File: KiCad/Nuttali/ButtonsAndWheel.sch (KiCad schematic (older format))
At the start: 17 parts, among them J3 Conn_01x03_Male, SW8 Rotary_Encoder, U6 Button, U7 Button, U8 Scroll_button, U9 Button

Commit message: Finnished design.
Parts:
- removed D4: LED, Nuttali:LED, symbol Nuttali-rescue:LED-Device
- added J4: Conn_01x02_Male, Connector_PinSocket_2.54mm:PinSocket_1x02_P2.54mm_Vertical, symbol Connector:Conn_01x02_Male
- added TP10, TP11, TP12, TP13, TP14, TP15: TestPoint, TestPoint:TestPoint_Pad_1.0x1.0mm, symbol Nuttali-rescue:TestPoint-Connector
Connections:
- net GND: now also J4.1 (Pin_1)
- net LeftB: now also TP10.1
- net RightB: now also TP11.1
- net Turbo: now also TP15.1
- net Turbo_LED: now also J4.2 (Pin_2)
- net WheelA: now also TP13.1
- net WheelB: now also TP14.1
- net WheelButton: now also TP12.1
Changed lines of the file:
@@
 Wire Wire Line
 	5000 2550 4950 2550
-Wire Wire Line
-	3900 2750 3800 2750
-Text GLabel 3800 2750 0    50   Output ~ 0
+Text GLabel 3650 2750 0    50   Output ~ 0
 WheelButton
 $Comp
@@
 $EndComp
 $Comp
-L Nuttali-rescue:LED-Device D4
-U 1 1 602CBCDE
-P 9600 2650
-F 0 "D4" H 9593 2395 50  0000 C CNN
-F 1 "LED" H 9593 2486 50  0000 C CNN
-F 2 "Nuttali:LED" H 9600 2650 50  0001 C CNN
-F 3 "~" H 9600 2650 50  0001 C CNN
-	1    9600 2650
-	-1   0    0    1
-$EndComp
-$Comp
 L Nuttali-rescue:GND-power #PWR0152
 U 1 1 602CF144
@@
 Text GLabel 9300 2650 0    50   Input ~ 0
 Turbo_LED
-Wire Wire Line
-	9300 2650 9450 2650
-Wire Wire Line
-	9750 2650 10100 2650
 Wire Wire Line
 	10100 2700 10100 2650
@@
 Connection ~ 1150 2950
 Wire Wire Line
-	1150 2950 850  2950
+	1150 2950 900  2950
 $Comp
 L Nuttali-rescue:R-Device R7
@@
 $EndComp
 Wire Wire Line
-	900  1350 1200 1350
+	900  1350 950  1350
 Connection ~ 1200 1350
 Wire Wire Line
@@
 	7000 6500 7000 500
 Wire Wire Line
-	9350 3400 9350 3850
+	9350 3400 9350 3700
 Connection ~ 4900 3200
 Wire Wire Line
-	4200 3200 4900 3200
+	4200 3200 4350 3200
 $Comp
 L Nuttali-rescue:+3.3V-power #PWR0146
@@
 Connection ~ 4900 4200
 Wire Wire Line
-	4200 4200 4900 4200
+	4200 4200 4750 4200
 $Comp
 L Nuttali-rescue:+3.3V-power #PWR0149
@@
 Wire Wire Line
 	5250 4200 5200 4200
+$Comp
+L Nuttali-rescue:TestPoint-Connector TP?
+U 1 1 602996E2
+P 950 1150
+AR Path="/601B1425/602996E2" Ref="TP?"  Part="1"
+AR Path="/6022DC9B/602996E2" Ref="TP11"  Part="1"
+F 0 "TP11" H 1008 1268 50  0000 L CNN
+F 1 "TestPoint" H 1008 1177 50  0000 L CNN
+F 2 "TestPoint:TestPoint_Pad_1.0x1.0mm" H 1150 1150 50  0001 C CNN
+F 3 "~" H 1150 1150 50  0001 C CNN
+	1    950  1150
+	1    0    0    -1
+$EndComp
+$Comp
+L Nuttali-rescue:TestPoint-Connector TP?
+U 1 1 6029A34F
+P 900 2750
+AR Path="/601B1425/6029A34F" Ref="TP?"  Part="1"
+AR Path="/6022DC9B/6029A34F" Ref="TP10"  Part="1"
+F 0 "TP10" H 958 2868 50  0000 L CNN
+F 1 "TestPoint" H 958 2777 50  0000 L CNN
+F 2 "TestPoint:TestPoint_Pad_1.0x1.0mm" H 1100 2750 50  0001 C CNN
+F 3 "~" H 1100 2750 50  0001 C CNN
+	1    900  2750
+	1    0    0    -1
+$EndComp
+$Comp
+L Nuttali-rescue:TestPoint-Connector TP?
+U 1 1 6029B953
+P 3750 2250
+AR Path="/601B1425/6029B953" Ref="TP?"  Part="1"
+AR Path="/6022DC9B/6029B953" Ref="TP12"  Part="1"
+F 0 "TP12" H 3808 2368 50  0000 L CNN
+F 1 "TestPoint" H 3808 2277 50  0000 L CNN
+F 2 "TestPoint:TestPoint_Pad_1.0x1.0mm" H 3950 2250 50  0001 C CNN
+F 3 "~" H 3950 2250 50  0001 C CNN
+	1    3750 2250
+	1    0    0    -1
+$EndComp
+$Comp
+L Nuttali-rescue:TestPoint-Connector TP?
+U 1 1 6029C224
+P 4350 3100
+AR Path="/601B1425/6029C224" Ref="TP?"  Part="1"
+AR Path="/6022DC9B/6029C224" Ref="TP13"  Part="1"
+F 0 "TP13" H 4408 3218 50  0000 L CNN
+F 1 "TestPoint" H 4408 3127 50  0000 L CNN
+F 2 "TestPoint:TestPoint_Pad_1.0x1.0mm" H 4550 3100 50  0001 C CNN
+F 3 "~" H 4550 3100 50  0001 C CNN
+	1    4350 3100
+	1    0    0    -1
+$EndComp
+$Comp
+L Nuttali-rescue:TestPoint-Connector TP?
+U 1 1 6029CEB2
+P 4750 4300
+AR Path="/601B1425/6029CEB2" Ref="TP?"  Part="1"
+AR Path="/6022DC9B/6029CEB2" Ref="TP14"  Part="1"
+F 0 "TP14" H 4808 4418 50  0000 L CNN
+F 1 "TestPoint" H 4808 4327 50  0000 L CNN
+F 2 "TestPoint:TestPoint_Pad_1.0x1.0mm" H 4950 4300 50  0001 C CNN
+F 3 "~" H 4950 4300 50  0001 C CNN
+	1    4750 4300
+	-1   0    0    1
+$EndComp
+$Comp
+L Nuttali-rescue:TestPoint-Connector TP?
+U 1 1 6029F887
+P 9500 3700
+AR Path="/601B1425/6029F887" Ref="TP?"  Part="1"
+AR Path="/6022DC9B/6029F887" Ref="TP15"  Part="1"
+F 0 "TP15" H 9558 3818 50  0000 L CNN
+F 1 "TestPoint" H 9558 3727 50  0000 L CNN
+F 2 "TestPoint:TestPoint_Pad_1.0x1.0mm" H 9700 3700 50  0001 C CNN
+F 3 "~" H 9700 3700 50  0001 C CNN
+	1    9500 3700
+	1    0    0    -1
+$EndComp
+Wire Wire Line
+	9500 3700 9350 3700
+Connection ~ 9350 3700
+Wire Wire Line
+	9350 3700 9350 3850
+Wire Wire Line
+	900  2950 900  2750
+Connection ~ 900  2950
+Wire Wire Line
+	900  2950 850  2950
+Wire Wire Line
+	950  1350 950  1150
+Connection ~ 950  1350
+Wire Wire Line
+	950  1350 1200 1350
+Wire Wire Line
+	3650 2750 3750 2750
+Wire Wire Line
+	3750 2250 3750 2750
+Connection ~ 3750 2750
+Wire Wire Line
+	3750 2750 3900 2750
+$Comp
+L Connector:Conn_01x02_Male J4
+U 1 1 602CAADB
+P 9650 2450
+F 0 "J4" V 9712 2494 50  0000 L CNN
+F 1 "Conn_01x02_Male" V 9803 2494 50  0000 L CNN
+F 2 "Connector_PinSocket_2.54mm:PinSocket_1x02_P2.54mm_Vertical" H 9650 2450 50  0001 C CNN
+F 3 "~" H 9650 2450 50  0001 C CNN
+	1    9650 2450
+	0    1    1    0
+$EndComp
+Wire Wire Line
+	9650 2650 10100 2650
+Wire Wire Line
+	9300 2650 9550 2650
+Wire Wire Line
+	4350 3100 4350 3200
+Connection ~ 4350 3200
+Wire Wire Line
+	4350 3200 4900 3200
+Wire Wire Line
+	4750 4300 4750 4200
+Connection ~ 4750 4200
+Wire Wire Line
+	4750 4200 4900 4200
 $EndSCHEMATC

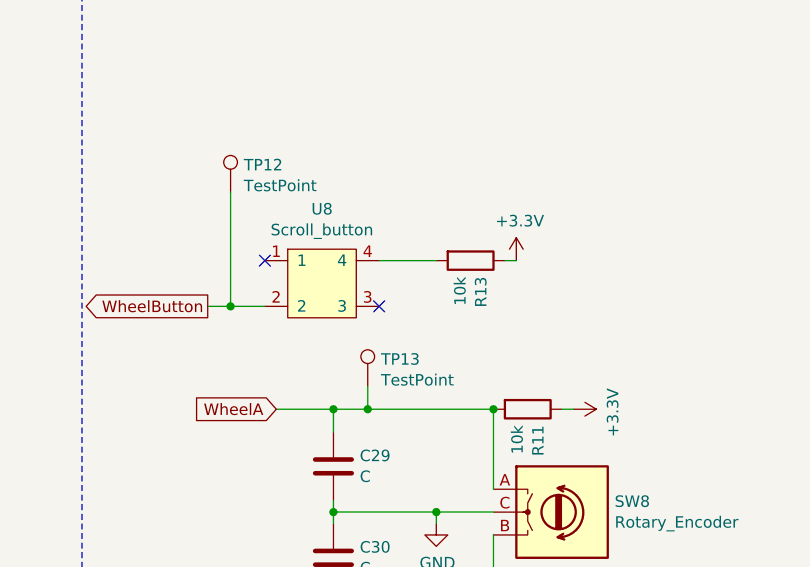
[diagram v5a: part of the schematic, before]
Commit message: Changed routes on the scroll wheel button
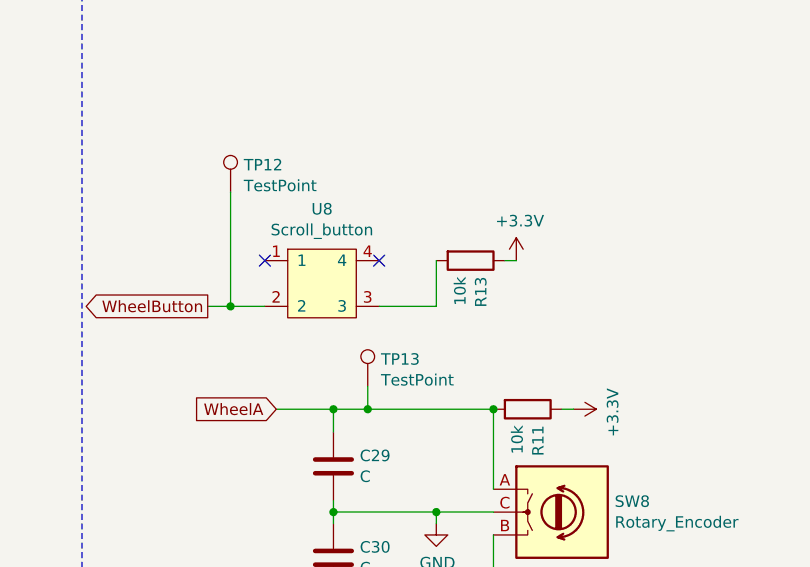
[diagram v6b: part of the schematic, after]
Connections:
- net at U8.3: now also R13.2
- net at U8.4: no longer R13.2
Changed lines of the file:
@@
 $EndComp
-Wire Wire Line
-	4400 2550 4650 2550
 Wire Wire Line
 	5000 2550 4950 2550
@@
 	1    0    0    -1
 $EndComp
-NoConn ~ 4400 2750
 NoConn ~ 3900 2550
 $Comp
@@
 Wire Wire Line
 	4750 4200 4900 4200
+Wire Wire Line
+	4650 2750 4400 2750
+Wire Wire Line
+	4650 2750 4650 2550
+NoConn ~ 4400 2550
 $EndSCHEMATC

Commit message: Last push befor ordering
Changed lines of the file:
@@
 	1    0    0    -1
 $EndComp
+NoConn ~ 4400 2550
 NoConn ~ 3900 2550
 $Comp
@@
 NoConn ~ 9500 3400
 Wire Notes Line
-	7000 6500 7000 500
+	7050 6650 7050 650
 Wire Wire Line
 	9350 3400 9350 3700
@@
 	4750 4200 4900 4200
 Wire Wire Line
-	4650 2750 4400 2750
-Wire Wire Line
-	4650 2750 4650 2550
-NoConn ~ 4400 2550
+	4400 2750 4550 2750
+Wire Wire Line
+	4550 2750 4550 2550
+Wire Wire Line
+	4550 2550 4650 2550
 $EndSCHEMATC

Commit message: added pers things to project
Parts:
- C27: value C -> unknown
- C28, C29, C30: value C -> 220nf +-20%
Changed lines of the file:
@@
 P 1150 3100
 F 0 "C28" H 850 3100 50  0000 L CNN
-F 1 "C" H 900 3000 50  0000 L CNN
+F 1 "220nf +-20%" H 900 3000 50  0000 L CNN
 F 2 "Capacitor_SMD:C_0805_2012Metric_Pad1.18x1.45mm_HandSolder" H 1188 2950 50  0001 C CNN
 F 3 "~" H 1150 3100 50  0001 C CNN
@@
 P 4200 3450
 F 0 "C29" H 4315 3496 50  0000 L CNN
-F 1 "C" H 4315 3405 50  0000 L CNN
+F 1 "220nf +-20%" H 4315 3405 50  0000 L CNN
 F 2 "Capacitor_SMD:C_0805_2012Metric_Pad1.18x1.45mm_HandSolder" H 4238 3300 50  0001 C CNN
 F 3 "~" H 4200 3450 50  0001 C CNN
@@
 P 4200 3850
 F 0 "C30" H 4315 3896 50  0000 L CNN
-F 1 "C" H 4315 3805 50  0000 L CNN
+F 1 "220nf +-20%" H 4315 3805 50  0000 L CNN
 F 2 "Capacitor_SMD:C_0805_2012Metric_Pad1.18x1.45mm_HandSolder" H 4238 3700 50  0001 C CNN
 F 3 "~" H 4200 3850 50  0001 C CNN
@@
 P 1200 1500
 F 0 "C27" H 1315 1546 50  0000 L CNN
-F 1 "C" H 1315 1455 50  0000 L CNN
+F 1 "unknown" H 1315 1455 50  0000 L CNN
 F 2 "Capacitor_SMD:C_0805_2012Metric_Pad1.18x1.45mm_HandSolder" H 1238 1350 50  0001 C CNN
 F 3 "~" H 1200 1500 50  0001 C CNN
